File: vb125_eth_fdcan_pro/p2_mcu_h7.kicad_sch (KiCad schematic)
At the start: 49 parts, among them J1 TAGconnect NL, M1 DM-OLED042-647, U1 STM32H725IGKx, X3 ECX-.327-CDX-1293

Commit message: Finish schematics.
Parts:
- added C81: 4.7uF, Capacitor_SMD:C_0603_1608Metric, symbol Device:C
- added C82: 100nF, Capacitor_SMD:C_0402_1005Metric, symbol Device:C
- added C83, C84: 12pF, Capacitor_SMD:C_0402_1005Metric, symbol Device:C
- added J6: MEM2061-01-188-00-A, vhrd_connector_gct:MEM2061, symbol Connector:Micro_SD_Card_Det2
- added J7: Conn_02x20_Pin, Connector_PinHeader_1.27mm:PinHeader_2x20_P1.27mm_Vertical_SMD, symbol vhrd_connector_generic:Conn_02x20_Pin
- added R9: 33R, Resistor_SMD:R_0402_1005Metric, symbol Device:R
- added R9 (x2): 10K, Resistor_SMD:R_0402_1005Metric, symbol Device:R
- added SW1: KSS331GLFS, vhrd_electromechanical:SW_KSS3, symbol Switch:SW_Push
- C10, C11, C12, C13, C14, C2, C20, C21, C22, C23, C24, C25, C26, C27, C28, C29, C30, C31, C32, C33, C34, C35, C36, C37, C8, C9: footprint (none) -> Capacitor_SMD:C_0402_1005Metric
- FB1: footprint (none) -> Inductor_SMD:L_0603_1608Metric
- R1: footprint (none) -> Resistor_SMD:R_0402_1005Metric
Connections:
- net +3V3_DCDC: now also C81.1, C82.1, J6.4 (VDD), J7.30 (Pin_30), J7.32 (Pin_32), R9.1, R9.1
- net +5V0_SYS: now also J7.34 (Pin_34), J7.36 (Pin_36)
- net BOOT0: now also J1.8
- net GND: now also C81.2, C82.2, C83.2, C84.2, J6.11 (SHIELD), J6.6 (VSS), J6.9 (DET_B), J7.10 (Pin_10), J7.11 (Pin_11), J7.20 (Pin_20), J7.21 (Pin_21), J7.24 (Pin_24), J7.3 (Pin_3), J7.31 (Pin_31), SW1.1
- net I2C3_SCL: now also J7.23 (Pin_23)
- net I2C3_SDA: now also J7.25 (Pin_25)
- net OCTOSPI_CLK: now also J7.22 (Pin_22)
- net OCTOSPI_DQS: now also J7.28 (Pin_28)
- net OCTOSPI_IO0: now also J7.2 (Pin_2)
- net OCTOSPI_IO1: now also J7.4 (Pin_4)
- net OCTOSPI_IO2: now also J7.6 (Pin_6)
- net OCTOSPI_IO3: now also J7.8 (Pin_8)
- net OCTOSPI_IO4: now also J7.12 (Pin_12)
- net OCTOSPI_IO5: now also J7.14 (Pin_14)
- net OCTOSPI_IO6: now also J7.16 (Pin_16)
- net OCTOSPI_IO7: now also J7.18 (Pin_18)
- net OCTOSPI_NCS: now also J7.26 (Pin_26)
- net SDMMC_CK: now also R9.1
- net SDMMC_CMD: now also J6.3 (CMD)
- net SDMMC_D0: now also J6.7 (DAT0)
- net SDMMC_D1: now also J6.8 (DAT1)
- net SDMMC_D2: now also J6.1 (DAT2)
- net SDMMC_D3: now also J6.2 (DAT3/CD)
- net SPI1_MISO: now also J7.5 (Pin_5)
- net SPI1_MOSI: now also J7.7 (Pin_7)
- net SPI1_NSS: now also J7.9 (Pin_9)
- net SPI1_SCK: now also J7.1 (Pin_1)
- net SPI2_MISO: now also J7.15 (Pin_15)
- net SPI2_MOSI: now also J7.17 (Pin_17)
- net SPI2_NSS: now also J7.19 (Pin_19)
- net SPI2_SCK: now also J7.13 (Pin_13)
- net USART1_RX: now also J7.29 (Pin_29)
- net USART1_TX: now also J7.27 (Pin_27)
- net USART2_RX: now also J7.35 (Pin_35)
- net USART2_TX: now also J7.33 (Pin_33)
- net USBFS_DP: now reaches U1.B15 (PA12)
- net USBFS_DM: now reaches U1.C15 (PA11)
- net ULPI_RST: now reaches U1.D8 (PG12)
- net BUTTON: now reaches U1.F15 (PG5)
- net BUTTON: now also R9.2, SW1.2
- net SDMMC_PRESENT: now reaches U1.G14 (PG4)
- net SDMMC_PRESENT: now also J6.10 (DET_A), R9.2
- net OSC32_OUT: now reaches U1.D1 (PC15-OSC32_OUT)
- net OSC32_OUT: now also X3.2, C83.1
- net OSC32_IN: now reaches U1.D2 (PC14-OSC32_IN)
- net OSC32_IN: now also X3.1, C84.1
- new net SDMMC_CKJ: J6.5 (CLK), R9.2
- no-connect marks 0 -> 58
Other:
- note added: "Button"
- note added: "MicroSD Card"
- note added: "RTC crystal"
- note added: "STM32H725IGKx"
- moved on the sheet: B1, C1, C10, C11, C12, C13, C14, C2, C20, C21, C22, C23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

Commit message: Add testpoints and set page templates.
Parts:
- added TP1, TP2, TP3: TestPoint_Probe, TestPoint:TestPoint_Pad_D1.5mm, symbol Connector:TestPoint_Probe
- renumbered C10 to C1, C1 to C10, C2 to C11, C20 to C12, C21 to C13, C22 to C14, C31 to C15, C23 to C16, C84 to C17, C32 to C18, C24 to C19, C11 to C2, C83 to C20, C25 to C21, C30 to C22, C26 to C23, C29 to C24, C36 to C25, C27 to C26, C34 to C27, C37 to C29, C12 to C3, C33 to C30, C35 to C31, C13 to C4, C14 to C5, C8 to C6, C9 to C7, C81 to C8, C82 to C9, J6 to J1, J1 to J2, J7 to J3, R1 to R7, X3 to X1
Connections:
- net I2C2_SCL: now also TP1.1
- net I2C2_SDA: now also TP2.1
- net VDDLDO: now also TP3.1
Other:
- company: vhrd.tech -> vhrd.tech AS
- title: STM32H725IGK -> rt_bridge_pro

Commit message: Add sourcing information for resistors
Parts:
- R7, R9: Mpn1 (none) -> RM04F1002CT; Mpn2 (none) -> RMCF0402FT10K0; Mpn3 (none) -> CR0402-FX-1002GLF
- R9: Mpn1 (none) -> RMCF0402FT3K30; Mpn2 (none) -> RC0402FR-073K3L
- R9: Mpn1 (none) -> CR0402-FX-33R0GLF; Mpn2 (none) -> RMCF0402FT33R0
- R9: Mpn1 (none) -> CR0402-FX-49R9GLF; Mpn2 (none) -> RMCF0402FT49R9
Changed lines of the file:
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@@
       (effects (font (size 1.27 1.27)) hide)
     )
+    (property "Mpn1" "RMCF0402FT3K30" (at 96.52 186.69 0)
+      (effects (font (size 1.27 1.27)) hide)
+    )
+    (property "Mpn2" "RC0402FR-073K3L" (at 96.52 186.69 0)
+      (effects (font (size 1.27 1.27)) hide)
+    )
     (pin "1")
     (pin "2")
@@
       (effects (font (size 1.27 1.27)) hide)
     )
+    (property "Mpn1" "CR0402-FX-33R0GLF" (at 213.36 256.54 0)
+      (effects (font (size 1.27 1.27)) hide)
+    )
+    (property "Mpn2" "RMCF0402FT33R0" (at 213.36 256.54 0)
+      (effects (font (size 1.27 1.27)) hide)
+    )
     (pin "1")
     (pin "2")
@@
       (effects (font (size 1.27 1.27)) hide)
     )
+    (property "Mpn1" "RM04F1002CT" (at 191.77 264.16 0)
+      (effects (font (size 1.27 1.27)) hide)
+    )
+    (property "Mpn2" "RMCF0402FT10K0" (at 191.77 264.16 0)
+      (effects (font (size 1.27 1.27)) hide)
+    )
+    (property "Mpn3" "CR0402-FX-1002GLF" (at 191.77 264.16 0)
+      (effects (font (size 1.27 1.27)) hide)
+    )
     (pin "1")
     (pin "2")
@@
       (effects (font (size 1.27 1.27)) hide)
     )
+    (property "Mpn1" "CR0402-FX-49R9GLF" (at 261.62 69.85 0)
+      (effects (font (size 1.27 1.27)) hide)
+    )
+    (property "Mpn2" "RMCF0402FT49R9" (at 261.62 69.85 0)
+      (effects (font (size 1.27 1.27)) hide)
+    )
     (pin "1")
     (pin "2")
@@
       (effects (font (size 1.27 1.27)) hide)
     )
+    (property "Mpn1" "RM04F1002CT" (at 165.1 173.99 0)
+      (effects (font (size 1.27 1.27)) hide)
+    )
+    (property "Mpn2" "RMCF0402FT10K0" (at 165.1 173.99 0)
+      (effects (font (size 1.27 1.27)) hide)
+    )
+    (property "Mpn3" "CR0402-FX-1002GLF" (at 165.1 173.99 0)
+      (effects (font (size 1.27 1.27)) hide)
+    )
     (pin "1")
     (pin "2")
@@
       (effects (font (size 1.27 1.27)) hide)
     )
+    (property "Mpn1" "RMCF0402FT3K30" (at 44.45 173.99 0)
+      (effects (font (size 1.27 1.27)) hide)
+    )
+    (property "Mpn2" "RC0402FR-073K3L" (at 44.45 173.99 0)
+      (effects (font (size 1.27 1.27)) hide)
+    )
     (pin "1")
     (pin "2")
@@
       (effects (font (size 1.27 1.27)) hide)
     )
+    (property "Mpn1" "RMCF0402FT3K30" (at 35.56 173.99 0)
+      (effects (font (size 1.27 1.27)) hide)
+    )
+    (property "Mpn2" "RC0402FR-073K3L" (at 35.56 173.99 0)
+      (effects (font (size 1.27 1.27)) hide)
+    )
     (pin "1")
     (pin "2")
@@
       (effects (font (size 1.27 1.27)) hide)
     )
+    (property "Mpn1" "RM04F1002CT" (at 312.42 236.22 0)
+      (effects (font (size 1.27 1.27)) hide)
+    )
+    (property "Mpn2" "RMCF0402FT10K0" (at 312.42 236.22 0)
+      (effects (font (size 1.27 1.27)) hide)
+    )
+    (property "Mpn3" "CR0402-FX-1002GLF" (at 312.42 236.22 0)
+      (effects (font (size 1.27 1.27)) hide)
+    )
     (pin "1")
     (pin "2")
@@
       (effects (font (size 1.27 1.27)) hide)
     )
+    (property "Mpn1" "RMCF0402FT3K30" (at 76.2 173.99 0)
+      (effects (font (size 1.27 1.27)) hide)
+    )
+    (property "Mpn2" "RC0402FR-073K3L" (at 76.2 173.99 0)
+      (effects (font (size 1.27 1.27)) hide)
+    )
     (pin "1")
     (pin "2")
@@
       (effects (font (size 1.27 1.27)) hide)
     )
+    (property "Mpn1" "RMCF0402FT3K30" (at 26.67 173.99 0)
+      (effects (font (size 1.27 1.27)) hide)
+    )
+    (property "Mpn2" "RC0402FR-073K3L" (at 26.67 173.99 0)
+      (effects (font (size 1.27 1.27)) hide)
+    )
     (pin "1")
     (pin "2")
@@
       (effects (font (size 1.27 1.27)) hide)
     )
+    (property "Mpn1" "RMCF0402FT3K30" (at 53.34 173.99 0)
+      (effects (font (size 1.27 1.27)) hide)
+    )
+    (property "Mpn2" "RC0402FR-073K3L" (at 53.34 173.99 0)
+      (effects (font (size 1.27 1.27)) hide)
+    )
     (pin "1")
     (pin "2")
@@
       (effects (font (size 1.27 1.27)) hide)
     )
+    (property "Mpn1" "RMCF0402FT3K30" (at 116.84 173.99 0)
+      (effects (font (size 1.27 1.27)) hide)
+    )
+    (property "Mpn2" "RC0402FR-073K3L" (at 116.84 173.99 0)
+      (effects (font (size 1.27 1.27)) hide)
+    )
     (pin "1")
     (pin "2")
@@
       (effects (font (size 1.27 1.27)) hide)
     )
+    (property "Mpn1" "RMCF0402FT3K30" (at 116.84 186.69 0)
+      (effects (font (size 1.27 1.27)) hide)
+    )
+    (property "Mpn2" "RC0402FR-073K3L" (at 116.84 186.69 0)
+      (effects (font (size 1.27 1.27)) hide)
+    )
     (pin "1")
     (pin "2")
@@
       (effects (font (size 1.27 1.27)) hide)
     )
+    (property "Mpn1" "RMCF0402FT3K30" (at 96.52 173.99 0)
+      (effects (font (size 1.27 1.27)) hide)
+    )
+    (property "Mpn2" "RC0402FR-073K3L" (at 96.52 173.99 0)
+      (effects (font (size 1.27 1.27)) hide)
+    )
     (pin "1")
     (pin "2")
@@
       (effects (font (size 1.27 1.27)) hide)
     )
+    (property "Mpn1" "RMCF0402FT3K30" (at 76.2 186.69 0)
+      (effects (font (size 1.27 1.27)) hide)
+    )
+    (property "Mpn2" "RC0402FR-073K3L" (at 76.2 186.69 0)
+      (effects (font (size 1.27 1.27)) hide)
+    )
     (pin "1")
     (pin "2")
@@
       (effects (font (size 1.27 1.27)) hide)
     )
+    (property "Mpn1" "RM04F1002CT" (at 77.47 237.49 0)
+      (effects (font (size 1.27 1.27)) hide)
+    )
+    (property "Mpn2" "RMCF0402FT10K0" (at 77.47 237.49 0)
+      (effects (font (size 1.27 1.27)) hide)
+    )
+    (property "Mpn3" "CR0402-FX-1002GLF" (at 77.47 237.49 0)
+      (effects (font (size 1.27 1.27)) hide)
+    )
     (pin "1")
     (pin "2")
@@
       (effects (font (size 1.27 1.27)) hide)
     )
+    (property "Mpn1" "RM04F1002CT" (at 307.34 220.98 0)
+      (effects (font (size 1.27 1.27)) hide)
+    )
+    (property "Mpn2" "RMCF0402FT10K0" (at 307.34 220.98 0)
+      (effects (font (size 1.27 1.27)) hide)
+    )
+    (property "Mpn3" "CR0402-FX-1002GLF" (at 307.34 220.98 0)
+      (effects (font (size 1.27 1.27)) hide)
+    )

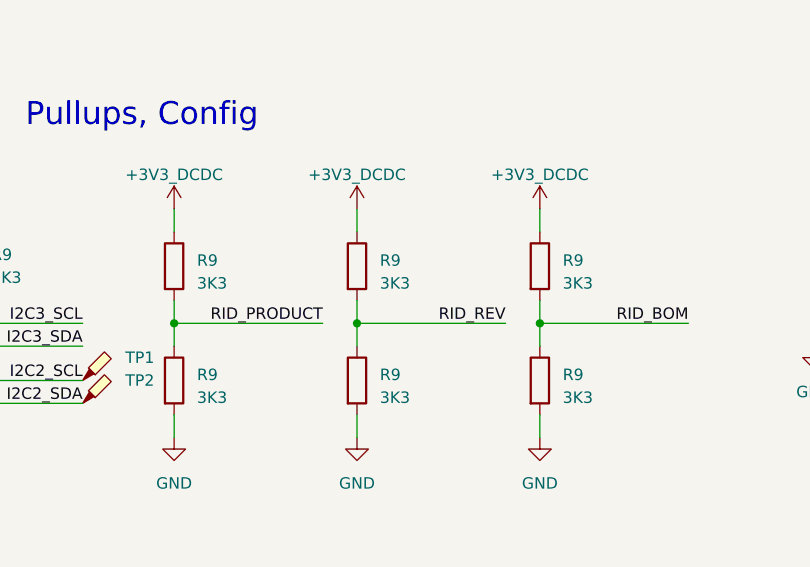
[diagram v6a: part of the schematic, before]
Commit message: Add variants.
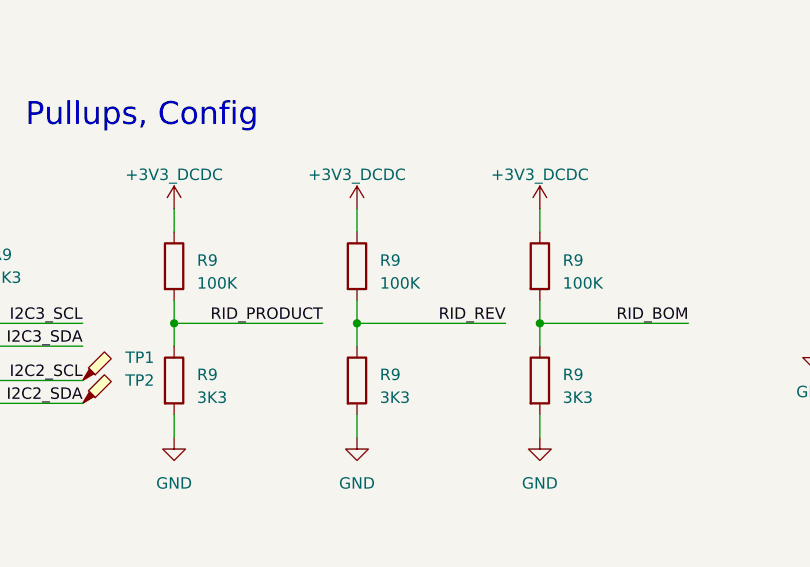
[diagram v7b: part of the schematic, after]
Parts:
- R9: value 3K3 -> 100K; Mpn1 RMCF0402FT3K30 -> (none); Mpn2 RC0402FR-073K3L -> (none)
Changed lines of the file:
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@@
       (effects (font (size 1.27 1.27)) (justify left))
     )
-    (property "Value" "3K3" (at 78.74 175.895 0)
+    (property "Value" "100K" (at 78.74 175.895 0)
       (effects (font (size 1.27 1.27)) (justify left))
     )
@@
       (effects (font (size 1.27 1.27)) hide)
     )
-    (property "Mpn1" "RMCF0402FT3K30" (at 76.2 173.99 0)
-      (effects (font (size 1.27 1.27)) hide)
-    )
-    (property "Mpn2" "RC0402FR-073K3L" (at 76.2 173.99 0)
+    (property "Mpn1" "" (at 76.2 173.99 0)
+      (effects (font (size 1.27 1.27)) hide)
+    )
+    (property "Mpn2" "" (at 76.2 173.99 0)
       (effects (font (size 1.27 1.27)) hide)
     )
@@
       (effects (font (size 1.27 1.27)) (justify left))
     )
-    (property "Value" "3K3" (at 119.38 175.895 0)
+    (property "Value" "100K" (at 119.38 175.895 0)
       (effects (font (size 1.27 1.27)) (justify left))
     )
@@
       (effects (font (size 1.27 1.27)) hide)
     )
-    (property "Mpn1" "RMCF0402FT3K30" (at 116.84 173.99 0)
-      (effects (font (size 1.27 1.27)) hide)
-    )
-    (property "Mpn2" "RC0402FR-073K3L" (at 116.84 173.99 0)
+    (property "Mpn1" "" (at 116.84 173.99 0)
+      (effects (font (size 1.27 1.27)) hide)
+    )
+    (property "Mpn2" "" (at 116.84 173.99 0)
       (effects (font (size 1.27 1.27)) hide)
     )
@@
       (effects (font (size 1.27 1.27)) (justify left))
     )
-    (property "Value" "3K3" (at 99.06 175.895 0)
+    (property "Value" "100K" (at 99.06 175.895 0)
       (effects (font (size 1.27 1.27)) (justify left))
     )
@@
       (effects (font (size 1.27 1.27)) hide)
     )
-    (property "Mpn1" "RMCF0402FT3K30" (at 96.52 173.99 0)
-      (effects (font (size 1.27 1.27)) hide)
-    )
-    (property "Mpn2" "RC0402FR-073K3L" (at 96.52 173.99 0)
-      (effects (font (size 1.27 1.27)) hide)
-    )
+    (property "Mpn1" "" (at 96.52 173.99 0)
+      (effects (font (size 1.27 1.27)) hide)
+    )
+    (property "Mpn2" "" (at 96.52 173.99 0)
+      (effects (font (size 1.27 1.27)) hide)
+    )

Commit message: Update p2_mcu_h7.kicad_sch
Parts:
- R9: value 3K3 -> RID_REV; Mpn1 RMCF0402FT3K30 -> (none); Mpn2 RC0402FR-073K3L -> (none)
- R9: value 3K3 -> RID_BOM; Mpn1 RMCF0402FT3K30 -> (none); Mpn2 RC0402FR-073K3L -> (none)
- R9: value 3K3 -> RID_PRODUCT; Mpn1 RMCF0402FT3K30 -> (none); Mpn2 RC0402FR-073K3L -> (none)
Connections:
- net +3V3_DCDC: no longer R9.1, R9.1, R9.1
- net RID_EN: now reaches U1.P5 (PA4)
- net RID_EN: now also R9.1, R9.1, R9.1
- no-connect marks 58 -> 57
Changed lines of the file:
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@@
   (junction (at 334.01 182.88) (diameter 0) (color 0 0 0 0)
   )
+  (junction (at 96.52 167.64) (diameter 0) (color 0 0 0 0)
+  )
   (junction (at 374.65 157.48) (diameter 0) (color 0 0 0 0)
   )
@@
   (junction (at 290.83 191.77) (diameter 0) (color 0 0 0 0)
   )
+  (junction (at 116.84 167.64) (diameter 0) (color 0 0 0 0)
+  )
   (junction (at 80.01 245.11) (diameter 0) (color 0 0 0 0)
   )
@@
   (no_connect (at 92.71 124.46))
   (no_connect (at 38.1 119.38))
-  (no_connect (at 38.1 43.18))
   (no_connect (at 200.66 58.42))
   (no_connect (at 368.3 77.47))
@@
     (stroke (width 0) (type default))
   )
+  (wire (pts (xy 38.1 43.18) (xy 71.12 43.18))
+    (stroke (width 0) (type default))
+  )
   (wire (pts (xy 22.86 267.97) (xy 22.86 270.51))
     (stroke (width 0) (type default))
@@
     (stroke (width 0) (type default))
   )
+  (wire (pts (xy 76.2 167.64) (xy 96.52 167.64))
+    (stroke (width 0) (type default))
+  )
   (wire (pts (xy 374.65 218.44) (xy 374.65 215.9))
     (stroke (width 0) (type default))
@@
     (stroke (width 0) (type default))
   )
+  (wire (pts (xy 116.84 167.64) (xy 133.35 167.64))
+    (stroke (width 0) (type default))
+  )
   (wire (pts (xy 269.24 143.51) (xy 275.59 143.51))
     (stroke (width 0) (type default))
@@
     (stroke (width 0) (type default))
   )
+  (wire (pts (xy 96.52 167.64) (xy 116.84 167.64))
+    (stroke (width 0) (type default))
+  )
   (wire (pts (xy 290.83 30.48) (xy 306.07 30.48))
     (stroke (width 0) (type default))
@@
     (effects (font (size 1.27 1.27) (color 194 0 194 1)) (justify right bottom))
   )
+  (label "RID_EN" (at 71.12 43.18 180) (fields_autoplaced)
+    (effects (font (size 1.27 1.27)) (justify right bottom))
+  )
   (label "BUTTON" (at 184.15 180.34 180) (fields_autoplaced)
     (effects (font (size 1.27 1.27)) (justify right bottom))
@@
     (effects (font (size 1.27 1.27)) (justify right bottom))
   )
+  (label "RID_EN" (at 133.35 167.64 180) (fields_autoplaced)
+    (effects (font (size 1.27 1.27)) (justify right bottom))
+  )
   (label "RID_PRODUCT" (at 92.71 180.34 180) (fields_autoplaced)
     (effects (font (size 1.27 1.27)) (justify right bottom))
@@
       (effects (font (size 1.27 1.27)) (justify left))
     )
-    (property "Value" "3K3" (at 99.06 188.595 0)
+    (property "Value" "RID_REV" (at 99.06 188.595 0)
       (effects (font (size 1.27 1.27)) (justify left))
     )
@@
       (effects (font (size 1.27 1.27)) hide)
     )
-    (property "Mpn1" "RMCF0402FT3K30" (at 96.52 186.69 0)
+    (property "Mpn1" "" (at 96.52 186.69 0)
       (effects (font (size 1.27 1.27)) hide)
     )
-    (property "Mpn2" "RC0402FR-073K3L" (at 96.52 186.69 0)
+    (property "Mpn2" "" (at 96.52 186.69 0)
       (effects (font (size 1.27 1.27)) hide)
     )
@@
     )
   )
-  (symbol (lib_id "vhrd_power:+3V3_DCDC") (at 116.84 167.64 0) (unit 1)
-    (in_bom yes) (on_board yes) (dnp no) (fields_autoplaced)
-    (property "Reference" "#PWR050" (at 120.65 168.91 0)
-      (effects (font (size 1.27 1.27)) hide)
-    )
-    (property "Value" "+3V3_DCDC" (at 116.84 163.83 0)
-      (effects (font (size 1.27 1.27)))
-    )
-    (property "Footprint" "" (at 116.84 167.64 0)
-      (effects (font (size 1.27 1.27)) hide)
-    )
-    (property "Datasheet" "" (at 116.84 167.64 0)
-      (effects (font (size 1.27 1.27)) hide)
-    )
-    (pin "1")
-    (instances
-      (project "vb125_eth_fdcan_pro"
-        (path "/b473bccb-f14c-41d5-b473-137d3ef8ae1e/6eaf8f36-f4c1-413f-846c-b502b7be2b8c"
-          (reference "#PWR050") (unit 1)
-        )
-        (path "/b473bccb-f14c-41d5-b473-137d3ef8ae1e/c16e79c7-955f-4686-8fe9-acff02e57751"
-          (reference "#PWR014") (unit 1)
-        )
-      )
-    )
-  )
   (symbol (lib_id "power:GND") (at 273.05 90.17 0) (unit 1)
     (in_bom yes) (on_board yes) (dnp no) (fields_autoplaced)
@@
     )
   )
-  (symbol (lib_id "vhrd_power:+3V3_DCDC") (at 96.52 167.64 0) (unit 1)
-    (in_bom yes) (on_board yes) (dnp no) (fields_autoplaced)
-    (property "Reference" "#PWR050" (at 100.33 168.91 0)
-      (effects (font (size 1.27 1.27)) hide)
-    )
-    (property "Value" "+3V3_DCDC" (at 96.52 163.83 0)
-      (effects (font (size 1.27 1.27)))
-    )
-    (property "Footprint" "" (at 96.52 167.64 0)
-      (effects (font (size 1.27 1.27)) hide)
-    )
-    (property "Datasheet" "" (at 96.52 167.64 0)
-      (effects (font (size 1.27 1.27)) hide)
-    )
-    (pin "1")
-    (instances
-      (project "vb125_eth_fdcan_pro"
-        (path "/b473bccb-f14c-41d5-b473-137d3ef8ae1e/6eaf8f36-f4c1-413f-846c-b502b7be2b8c"
-          (reference "#PWR050") (unit 1)
-        )
-        (path "/b473bccb-f14c-41d5-b473-137d3ef8ae1e/c16e79c7-955f-4686-8fe9-acff02e57751"
-          (reference "#PWR012") (unit 1)
-        )
-      )
-    )
-  )
   (symbol (lib_id "power:GND") (at 381 134.62 0) (unit 1)
     (in_bom yes) (on_board yes) (dnp no) (fields_autoplaced)
@@
     )
   )
-  (symbol (lib_id "vhrd_power:+3V3_DCDC") (at 76.2 167.64 0) (unit 1)
-    (in_bom yes) (on_board yes) (dnp no) (fields_autoplaced)
-    (property "Reference" "#PWR050" (at 80.01 168.91 0)
-      (effects (font (size 1.27 1.27)) hide)
-    )
-    (property "Value" "+3V3_DCDC" (at 76.2 163.83 0)
-      (effects (font (size 1.27 1.27)))
-    )
-    (property "Footprint" "" (at 76.2 167.64 0)
-      (effects (font (size 1.27 1.27)) hide)
-    )
-    (property "Datasheet" "" (at 76.2 167.64 0)
-      (effects (font (size 1.27 1.27)) hide)
-    )
-    (pin "1")
-    (instances
-      (project "vb125_eth_fdcan_pro"
-        (path "/b473bccb-f14c-41d5-b473-137d3ef8ae1e/6eaf8f36-f4c1-413f-846c-b502b7be2b8c"
-          (reference "#PWR050") (unit 1)
-        )
-        (path "/b473bccb-f14c-41d5-b473-137d3ef8ae1e/c16e79c7-955f-4686-8fe9-acff02e57751"
-          (reference "#PWR09") (unit 1)
-        )
-      )
-    )
-  )
   (symbol (lib_id "power:GND") (at 275.59 157.48 0) (unit 1)
     (in_bom yes) (on_board yes) (dnp no) (fields_autoplaced)
@@
       (effects (font (size 1.27 1.27)) (justify left))
     )
-    (property "Value" "3K3" (at 119.38 188.595 0)
+    (property "Value" "RID_BOM" (at 119.38 188.595 0)
       (effects (font (size 1.27 1.27)) (justify left))
     )
@@
       (effects (font (size 1.27 1.27)) hide)
     )
-    (property "Mpn1" "RMCF0402FT3K30" (at 116.84 186.69 0)
+    (property "Mpn1" "" (at 116.84 186.69 0)
       (effects (font (size 1.27 1.27)) hide)
     )
-    (property "Mpn2" "RC0402FR-073K3L" (at 116.84 186.69 0)
+    (property "Mpn2" "" (at 116.84 186.69 0)
       (effects (font (size 1.27 1.27)) hide)
     )
@@
       (effects (font (size 1.27 1.27)) (justify left))
     )
-    (property "Value" "3K3" (at 78.74 188.595 0)
+    (property "Value" "RID_PRODUCT" (at 78.74 188.595 0)
       (effects (font (size 1.27 1.27)) (justify left))
     )
@@
       (effects (font (size 1.27 1.27)) hide)
     )
-    (property "Mpn1" "RMCF0402FT3K30" (at 76.2 186.69 0)
+    (property "Mpn1" "" (at 76.2 186.69 0)
       (effects (font (size 1.27 1.27)) hide)
     )
-    (property "Mpn2" "RC0402FR-073K3L" (at 76.2 186.69 0)
+    (property "Mpn2" "" (at 76.2 186.69 0)
       (effects (font (size 1.27 1.27)) hide)
     )
